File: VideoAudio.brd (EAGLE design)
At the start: 106.7 x 82.2 mm, 33 parts, among them IC1 MAX734CPA, IC2 MAX660CPA, IC3 TMS9918A, Q1 10.738635MHz, T1 2N3904, X1 TOBU3

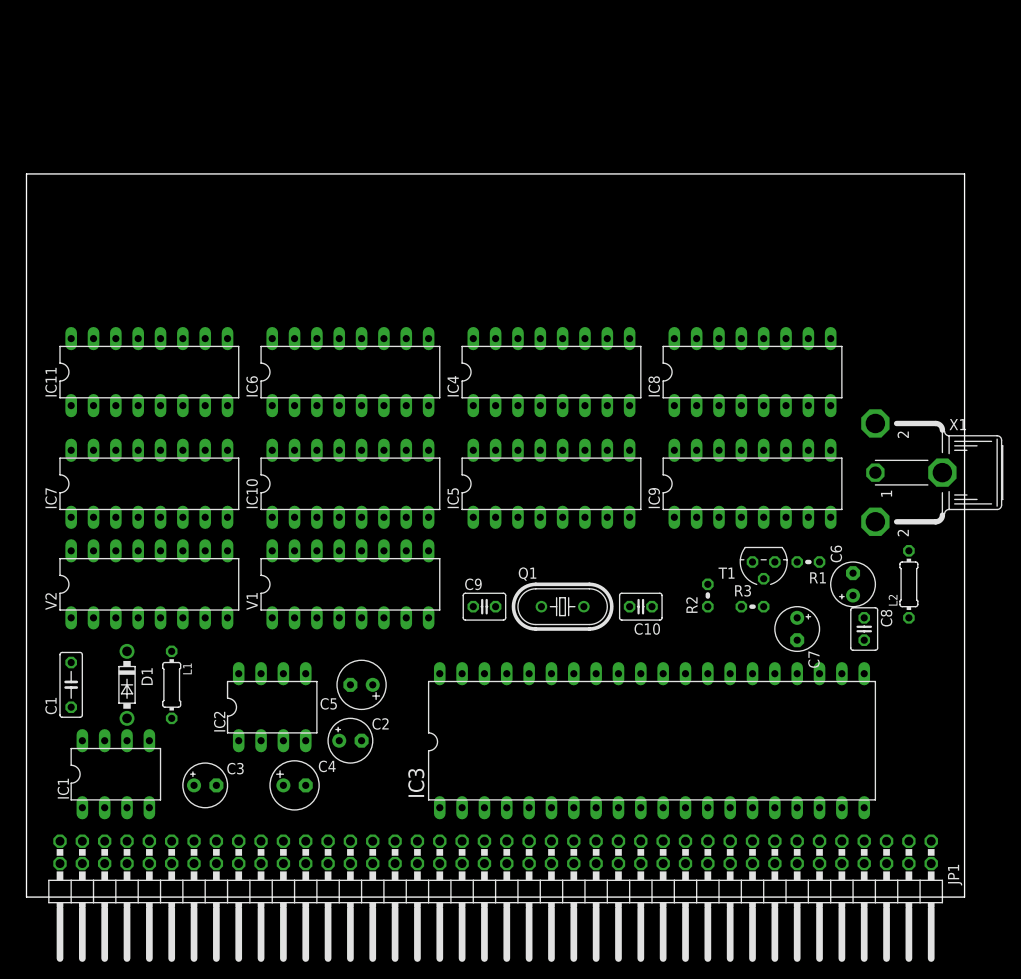
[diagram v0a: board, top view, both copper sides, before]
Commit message: Add Audio and Video to videoboard, not yet ready
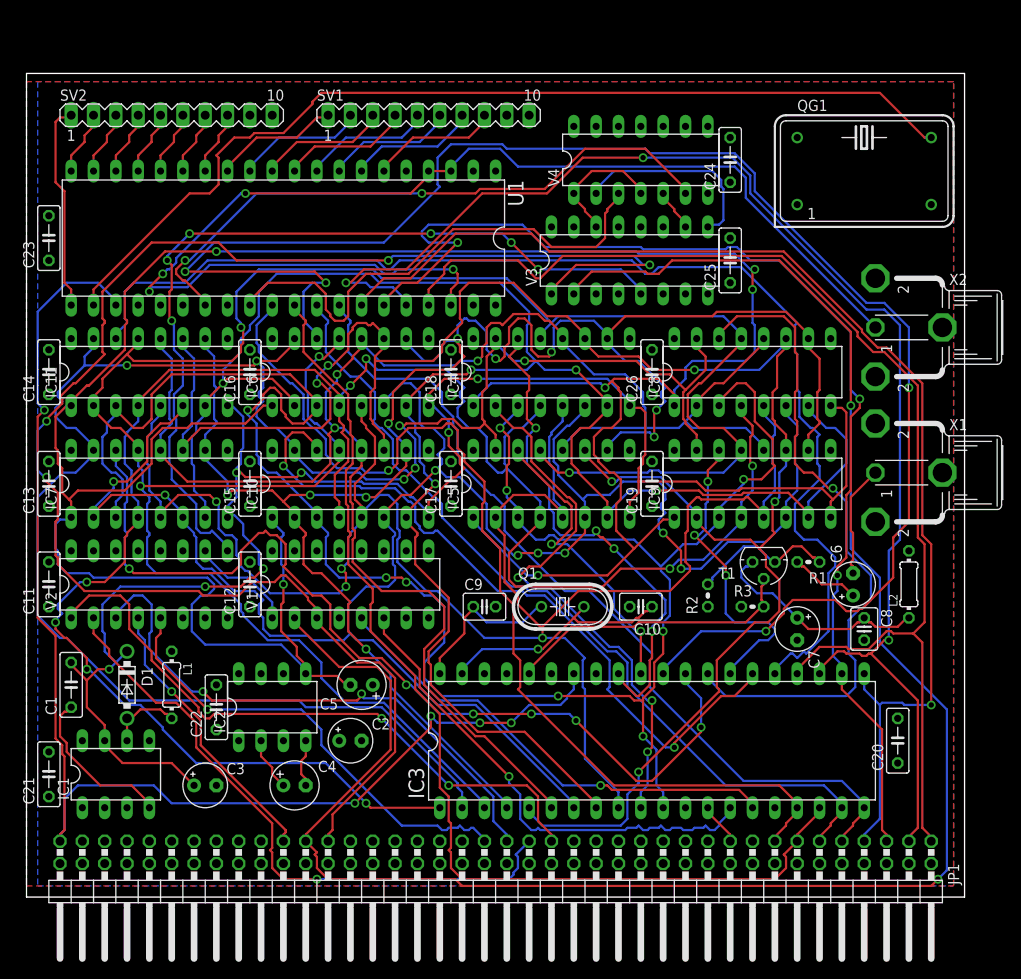
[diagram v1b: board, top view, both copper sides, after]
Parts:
- added C11, C12, C13, C14, C15, C16, C17, C18, C19, C20, C21, C22, C23, C24, C25, C26: 10µF, rcl:C050-025X075
- added QG1: 2MHz, crystal:DIL14S
- added SV1, SV2: (no value), con-lstb:MA10-1
- added U1: AY-3-8912, oldchips:DIL40
- added V3: 74238N, 74ttl-din:DIL16
- added V4: 7432N, 74ttl-din:DIL14
- added X2: TOBU3, con-hirschmann:TOBU3
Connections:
- new net !RESET: IC3.34, JP1.79, U1.23
- new net A0: V3.3
- new net N$11: V3.9, V4.2
- new net N$15: U1.29, V4.3
- new net N$16: V3.14, V4.1, V4.4
- new net N$17: U1.27, V4.6
- new net N$18: V3.10, V4.5
- new net N$19: SV1.1, U1.13
- new net N$20: SV1.2, U1.12
- new net N$21: SV1.3, U1.11
- new net N$22: SV1.4, U1.10
- new net N$23: SV1.5, U1.9
- new net N$24: SV1.6, U1.8
- new net N$25: SV1.7, U1.7
- new net N$26: SV1.8, U1.6
- new net N$27: QG1.8, U1.22
- new net N$28: SV2.1, U1.21
- new net N$29: SV2.2, U1.20
- new net N$30: SV2.3, U1.19
- new net N$31: SV2.4, U1.18
- new net N$32: SV2.5, U1.17
- new net N$33: SV2.6, U1.16
- new net N$34: SV2.7, U1.15
- new net N$35: SV2.8, U1.14
- net !AUDIOEN: now also V3.5
- net !RD: now also V3.1
- net !WR: now also V3.2
- net D0: now also U1.37
- net D1: now also U1.36
- net D2: now also U1.35
- net D3: now also U1.34
- net D4: now also U1.33
- net D5: now also U1.32
- net D6: now also U1.31
- net D7: now also U1.30
- net GND: now also QG1.7, SV1.10, SV2.10, U1.1, V3.4, V3.8, V4.7, X2.2, X2.2@1, X2.2@2
- net N$6: now also U1.3, U1.38, U1.4, X2.1; no longer IC3.34, JP1.79
- net VCC: now also C11.1, C12.1, C13.1, C14.1, C15.1, C16.1, C17.1, C18.1, C19.1, C20.1, C21.1, C22.1, C23.1, C24.1, C25.1, C26.1, QG1.14, SV1.9, SV2.9, U1.28, U1.40, V3.16, V3.6, V4.14
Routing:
- net -5V: track 0.00 -> 309.5 mm, vias 0 -> 6
- net AD7: track 0.00 -> 256.2 mm, vias 0 -> 4
- net !RAS: track 0.00 -> 229.8 mm, vias 0 -> 8
- net AD5: track 0.00 -> 229.4 mm, vias 0 -> 6
- net AD3: track 0.00 -> 229.4 mm, vias 0 -> 8
- net AD2: track 0.00 -> 228.8 mm, vias 0 -> 5
- net !W: track 0.00 -> 228.8 mm, vias 0 -> 9
- net !CAS: track 0.00 -> 222.9 mm, vias 0 -> 6
- net AD1: track 0.00 -> 217.4 mm, vias 0 -> 4
- net !WR: track 0.00 -> 216.1 mm, vias 0 -> 2
- net AD6: track 0.00 -> 215.6 mm, vias 0 -> 10
- net AD4: track 0.00 -> 199.6 mm, vias 0 -> 3
- net +12V: track 0.00 -> 199.2 mm, vias 0 -> 7
- net RD2: track 0.00 -> 187.4 mm, vias 0 -> 4
- net !RD: track 0.00 -> 183.3 mm, vias 0 -> 4
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- added copper zone on layer 16, net GND
- added copper zone on layer 1, net VCC
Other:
- board size 106.7 x 82.2 mm -> 106.7 x 93.7 mm

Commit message: Route Audio/Video Board
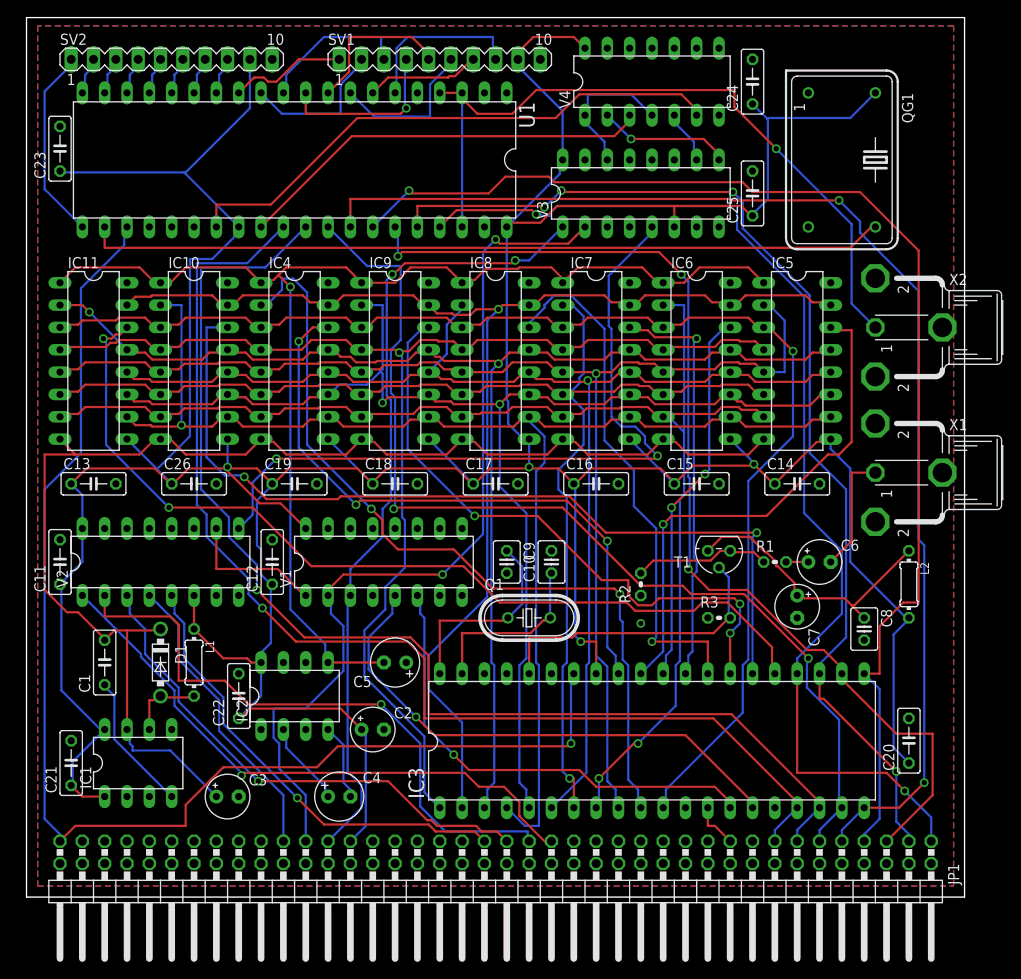
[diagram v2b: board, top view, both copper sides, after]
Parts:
- moved C14 86.0 mm to (86.4, 47.0), turned to 0 degrees
- moved C26 53.6 mm to (17.8, 47.0), turned to 0 degrees
- moved IC7 52.7 mm to (63.5, 61.0), turned to 270 degrees
- moved C15 50.8 mm to (74.9, 47.0), turned to 0 degrees
- moved IC9 43.0 mm to (40.6, 61.0), turned to 270 degrees
- moved C16 41.4 mm to (63.5, 47.0), turned to 0 degrees
- moved C19 40.6 mm to (29.2, 47.0), turned to 0 degrees
- moved IC6 39.4 mm to (74.9, 61.0), turned to 270 degrees
- moved IC5 31.2 mm to (86.4, 61.0), turned to 270 degrees
- moved IC4 29.2 mm to (29.2, 61.0), turned to 270 degrees
- moved IC8 29.2 mm to (52.1, 61.0), turned to 270 degrees
- moved IC10 22.6 mm to (17.8, 61.0), turned to 270 degrees
- moved C18 14.2 mm to (40.6, 47.0), turned to 0 degrees
- moved C10 11.4 mm to (58.4, 38.1), turned to 90 degrees
- moved C23 10.2 mm to (2.54, 85.1)
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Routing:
- net VCC: track 0.00 -> 523.8 mm, vias 0 -> 4
- net -5V: track 309.5 -> 144.0 mm, vias 6 -> 1
- net RD2: track 187.4 -> 42.9 mm, vias 4 -> 2
- net !WR: track 216.1 -> 101.7 mm
- net AD7: track 256.2 -> 151.8 mm, vias 4 -> 2
- net !RD: track 183.3 -> 90.8 mm, vias 4 -> 2
- net !RAS: track 229.8 -> 146.0 mm, vias 8 -> 1
- net !W: track 228.8 -> 149.2 mm, vias 9 -> 1
- net AD5: track 229.4 -> 150.9 mm, vias 6 -> 2
- net AD3: track 229.4 -> 152.5 mm, vias 8 -> 1
- net !CAS: track 222.9 -> 148.3 mm, vias 6 -> 1
- net AD2: track 228.8 -> 155.2 mm, vias 5 -> 2
- net AD1: track 217.4 -> 148.9 mm, vias 4 -> 1
- net RD3: track 107.7 -> 47.0 mm, vias 6 -> 1
- net AD6: track 215.6 -> 155.3 mm, vias 10 -> 1
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- added copper zone on layer 1, net GND
- removed copper zone on layer 1, net VCC
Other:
- board size 106.7 x 93.7 mm -> 106.7 x 100 mm
